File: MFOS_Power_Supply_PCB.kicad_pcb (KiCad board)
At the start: 2 copper layers, 110 x 40.9 mm, 29 parts, among them J1 9VAC~, J2 9VAC~, J3 GND, J4 +5VDC, J5 -5VDC, M1 MountingHole_3.2mm_M3_DIN965_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, M2 MountingHole_3.2mm_M3_DIN965_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, M3 MountingHole_3.2mm_M3_DIN965_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, M4 MountingHole_3.2mm_M3_DIN965_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, U1 LM7805_TO220, U2 LM7905_TO220

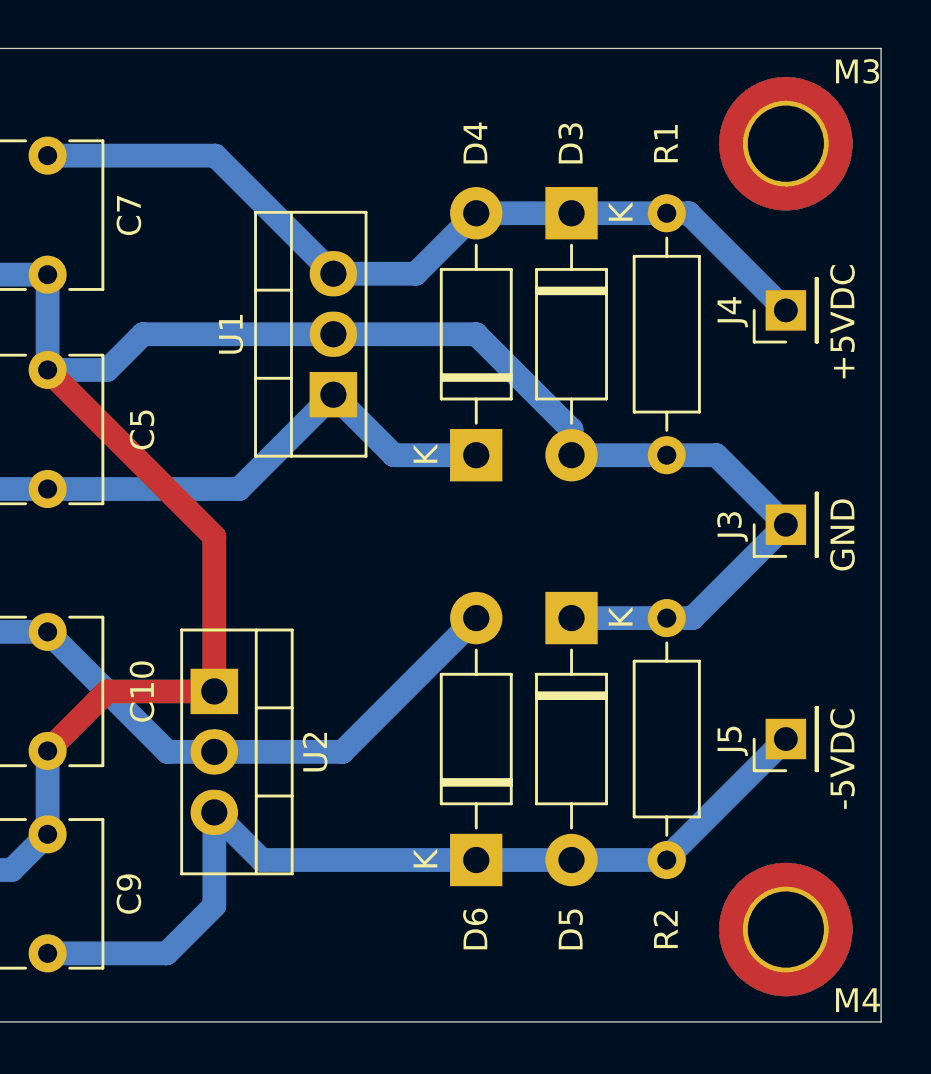
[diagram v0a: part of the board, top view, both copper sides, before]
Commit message: Added Silkscreen Titles
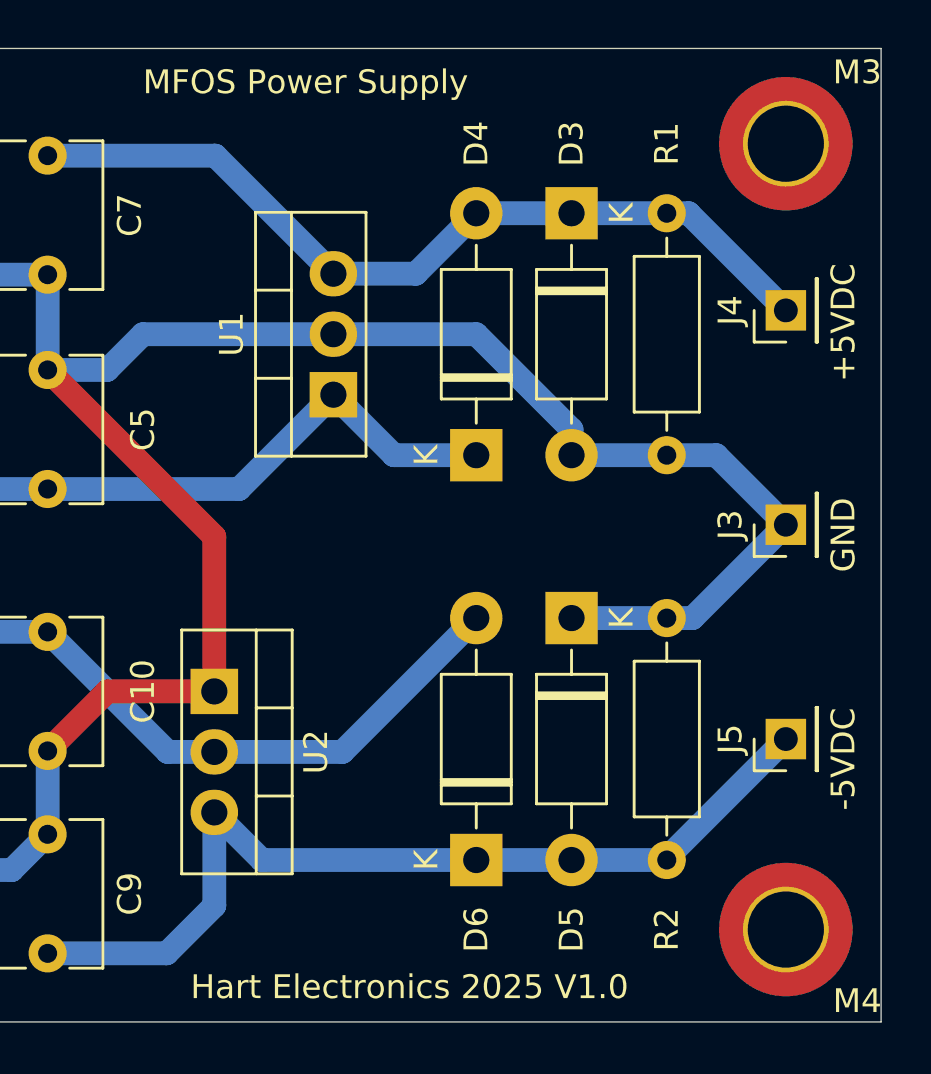
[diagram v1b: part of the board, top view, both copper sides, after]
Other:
- board text added: "Hart Electronics 2025 V1.0"
- board text added: "MFOS Power Supply"
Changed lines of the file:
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@@
 		(layer "Edge.Cuts")
+	)
+	(gr_text "Hart Electronics 2025 V1.0"
+		(at 140 94 0)
+		(layer "B.SilkS")
+		(effects
+			(font
+				(size 1 1)
+				(thickness 0.1)
+			)
+			(justify left bottom mirror)
+		)
+	)
+	(gr_text "MFOS Power Supply"
+		(at 137 92 0)
+		(layer "B.SilkS")
+		(effects
+			(font
+				(size 1 1)
+				(thickness 0.1)
+			)
+			(justify left bottom mirror)
+		)
+	)
+	(gr_text "MFOS Power Supply"
+		(at 168 74 0)
+		(layer "F.SilkS")
+		(effects
+			(font
+				(size 1 1)
+				(thickness 0.1)
+			)
+			(justify left bottom)
+		)
+	)
+	(gr_text "Hart Electronics 2025 V1.0"
+		(at 170 112 0)
+		(layer "F.SilkS")
+		(effects
+			(font
+				(size 1 1)
+				(thickness 0.1)
+			)
+			(justify left bottom)
+		)
 	)
 	(gr_text "9VAC~"
